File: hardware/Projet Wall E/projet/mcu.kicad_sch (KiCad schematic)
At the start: 21 parts, among them J301 Conn_ST_STDC14, J302 Conn_01x03, U301 STM32G431RBTx, Y301 16MHz

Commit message: verification finale effectue
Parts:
- added C313: 1u, Capacitor_SMD:C_0402_1005Metric, symbol wall_e:C
- C301, C302, C303, C304: value 100nF -> 100n
- C305: value 4.7u -> 4u7
- C307, C312: value 1uF -> 1u
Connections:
- net +5V_USB: now also C313.1
- net GND: now also C313.2
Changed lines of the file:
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@@
 	)
 	(junction
+		(at 238.76 139.7)
+		(diameter 0)
+		(color 0 0 0 0)
+	)
+	(junction
 		(at 29.21 64.77)
 		(diameter 0)
@@
 		(color 0 0 0 0)
 	)
+	(junction
+		(at 229.87 129.54)
+		(diameter 0)
+		(color 0 0 0 0)
+	)
 	(no_connect
 		(at 147.32 99.06)
@@
 	(wire
 		(pts
-			(xy 238.76 132.08) (xy 238.76 137.16)
+			(xy 238.76 132.08) (xy 238.76 139.7)
 		)
 		(stroke
@@
 	(wire
 		(pts
+			(xy 229.87 129.54) (xy 229.87 130.81)
+		)
+		(stroke
+			(width 0)
+			(type default)
+		)
+	)
+	(wire
+		(pts
 			(xy 160.02 45.72) (xy 143.51 45.72)
 		)
@@
 	(wire
 		(pts
+			(xy 229.87 138.43) (xy 229.87 139.7)
+		)
+		(stroke
+			(width 0)
+			(type default)
+		)
+	)
+	(wire
+		(pts
 			(xy 242.57 85.09) (xy 242.57 86.36)
 		)
@@
 	(wire
 		(pts
+			(xy 238.76 139.7) (xy 238.76 140.97)
+		)
+		(stroke
+			(width 0)
+			(type default)
+		)
+	)
+	(wire
+		(pts
 			(xy 123.19 92.71) (xy 127 92.71)
 		)
@@
 	(wire
 		(pts
-			(xy 243.84 129.54) (xy 224.79 129.54)
+			(xy 243.84 129.54) (xy 229.87 129.54)
 		)
 		(stroke
@@
 	(wire
 		(pts
+			(xy 229.87 129.54) (xy 224.79 129.54)
+		)
+		(stroke
+			(width 0)
+			(type default)
+		)
+	)
+	(wire
+		(pts
 			(xy 186.69 83.82) (xy 182.88 83.82)
 		)
@@
 	(wire
 		(pts
+			(xy 229.87 139.7) (xy 238.76 139.7)
+		)
+		(stroke
+			(width 0)
+			(type default)
+		)
+	)
+	(wire
+		(pts
 			(xy 102.87 87.63) (xy 102.87 97.79)
 		)
@@
 	)
 	(hierarchical_label "CHG_OTG"
-		(shape output)
+		(shape input)
 		(at 186.69 144.78 0)
 		(effects
@@
 			)
 		)
-		(property "Value" "1uF"
+		(property "Value" "1u"
 			(at 104.14 57.1499 0)
 			(show_name no)
@@
 	(symbol
 		(lib_id "power:GND")
-		(at 238.76 137.16 0)
+		(at 238.76 140.97 0)
 		(unit 1)
 		(body_style 1)
@@
 		(fields_autoplaced yes)
 		(property "Reference" "#PWR0309"
-			(at 238.76 143.51 0)
+			(at 238.76 147.32 0)
 			(hide yes)
 			(show_name no)
@@
 		)
 		(property "Value" "GND"
-			(at 238.76 142.24 0)
+			(at 238.76 146.05 0)
 			(show_name no)
 			(do_not_autoplace no)
@@
 		)
 		(property "Footprint" ""
-			(at 238.76 137.16 0)
+			(at 238.76 140.97 0)
 			(hide yes)
 			(show_name no)
@@
 		)
 		(property "Datasheet" ""
-			(at 238.76 137.16 0)
+			(at 238.76 140.97 0)
 			(hide yes)
 			(show_name no)
@@
 		)
 		(property "Description" "Power symbol creates a global label with name \"GND\" , ground"
-			(at 238.76 137.16 0)
+			(at 238.76 140.97 0)
 			(hide yes)
 			(show_name no)
@@
 			)
 		)
-		(property "Value" "100nF"
+		(property "Value" "100n"
 			(at 33.02 57.1499 0)
 			(show_name no)
@@
 			)
 		)
-		(property "Value" "100nF"
+		(property "Value" "100n"
 			(at 60.96 57.1499 0)
 			(show_name no)
@@
 	(symbol
 		(lib_id "wall_e:C")
+		(at 229.87 134.62 0)
+		(unit 1)
+		(body_style 1)
+		(exclude_from_sim no)
+		(in_bom yes)
+		(on_board yes)
+		(in_pos_files yes)
+		(dnp no)
+		(fields_autoplaced yes)
+		(property "Reference" "C313"
+			(at 233.68 133.3499 0)
+			(show_name no)
+			(do_not_autoplace no)
+			(effects
+				(font
+					(size 1.27 1.27)
+				)
+				(justify left)
+			)
+		)
+		(property "Value" "1u"
+			(at 233.68 135.8899 0)
+			(show_name no)
+			(do_not_autoplace no)
+			(effects
+				(font
+					(size 1.27 1.27)
+				)
+				(justify left)
+			)
+		)
+		(property "Footprint" "Capacitor_SMD:C_0402_1005Metric"
+			(at 230.8352 138.43 0)
+			(hide yes)
+			(show_name no)
+			(do_not_autoplace no)
+			(effects
+				(font
+					(size 1.27 1.27)
+				)
+			)
+		)
+		(property "Datasheet" ""
+			(at 229.87 134.62 0)
+			(hide yes)
+			(show_name no)
+			(do_not_autoplace no)
+			(effects
+				(font
+					(size 1.27 1.27)
+				)
+			)
+		)
+		(property "Description" "Unpolarized capacitor"
+			(at 229.87 134.62 0)
+			(hide yes)
+			(show_name no)
+			(do_not_autoplace no)
+			(effects
+				(font
+					(size 1.27 1.27)
+				)
+			)
+		)
+		(property "JLCPCB Part#" "C52923"
+			(at 229.87 134.62 0)
+			(hide yes)
+			(show_name no)
+			(do_not_autoplace no)
+			(effects
+				(font
+					(size 1.27 1.27)
+				)
+			)
+		)
+		(property "KLC_S3.3" ""
+			(at 229.87 134.62 0)
+			(hide yes)
+			(show_name no)
+			(do_not_autoplace no)
+			(effects
+				(font
+					(size 1.27 1.27)
+				)
+			)
+		)
+		(property "KLC_S4.1" ""
+			(at 229.87 134.62 0)
+			(hide yes)
+			(show_name no)
+			(do_not_autoplace no)
+			(effects
+				(font
+					(size 1.27 1.27)
+				)
+			)
+		)
+		(property "Sim.Device" ""
+			(at 229.87 134.62 0)
+			(hide yes)
+			(show_name no)
+			(do_not_autoplace no)
+			(effects
+				(font
+					(size 1.27 1.27)
+				)
+			)
+		)
+		(pin "2"
+		)
+		(pin "1"
+		)
+		(instances
+			(project "projet"
+				(path "/aad9219d-d686-4d68-8dbb-b3c2b0727159/8d7235a3-ed0d-4c0c-a716-b22c65fe70a8"
+					(reference "C313")
+					(unit 1)
+				)
+			)
+		)
+	)
+	(symbol
+		(lib_id "wall_e:C")
 		(at 43.18 55.88 0)
 		(unit 1)
@@
 			)
 		)
-		(property "Value" "100nF"
+		(property "Value" "100n"
 			(at 46.99 57.1499 0)
 			(show_name no)
@@
 			)
 		)
-		(property "Value" "100nF"
+		(property "Value" "100n"
 			(at 19.05 57.1499 0)
 			(show_name no)
@@
 			)
 		)
-		(property "Value" "4.7u"
+		(property "Value" "4u7"
 			(at 76.2 57.1499 0)
 			(show_name no)
@@
 			)
 		)
-		(property "Value" "1uF"
+		(property "Value" "1u"
 			(at 130.81 57.1499 0)
 			(show_name no)

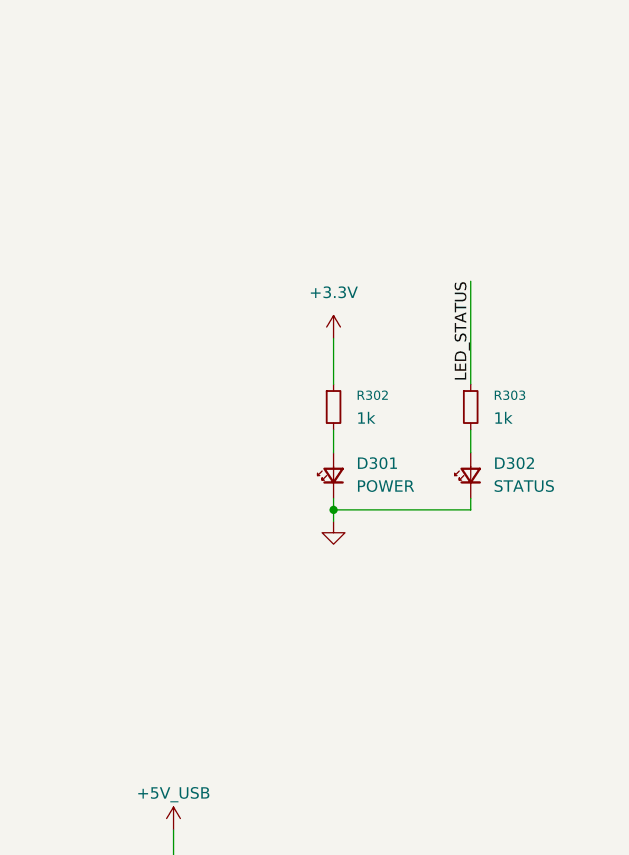
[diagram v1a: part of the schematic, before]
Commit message: PCB : contour 80x40, trous de fixation M2.5, sérigraphie
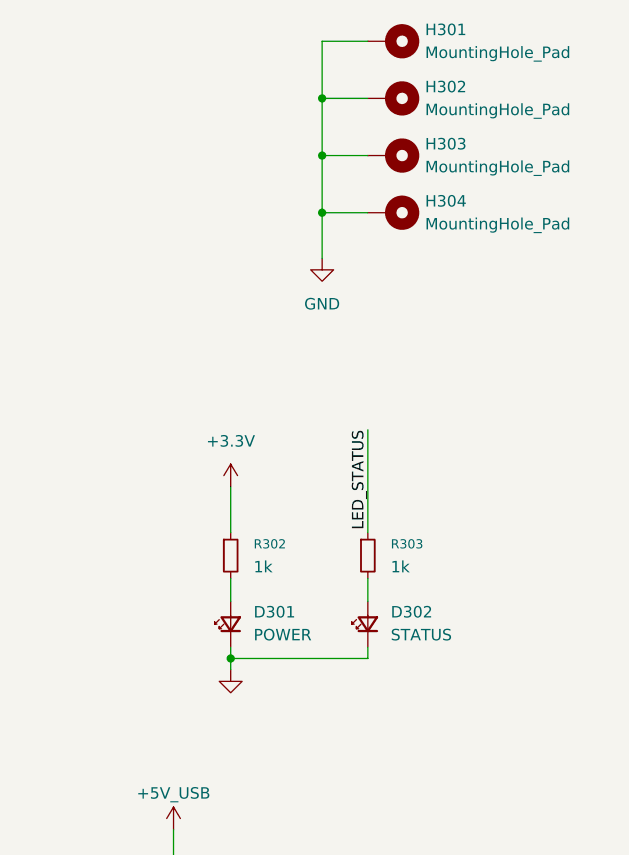
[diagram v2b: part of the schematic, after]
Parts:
- added H301, H302, H303, H304: MountingHole_Pad, MountingHole:MountingHole_2.2mm_M2_Pad_Via, symbol Mechanical:MountingHole_Pad
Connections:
- net GND: now also H301.1, H302.1, H303.1, H304.1
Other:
- moved on the sheet: D301, D302, R302, R303

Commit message: PCB : placement final avant routage
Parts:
- J301: JLCPCB Part# C2935955 -> C7465995
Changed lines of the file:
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@@
 			)
 		)
-		(property "JLCPCB Part#" "C2935955"
+		(property "JLCPCB Part#" "C7465995"
 			(at 57.15 120.65 0)
 			(hide yes)
